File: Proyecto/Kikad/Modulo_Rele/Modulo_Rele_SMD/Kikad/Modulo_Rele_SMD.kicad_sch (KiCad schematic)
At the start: 8 parts, among them J1 TB_1X3, J2 TB_1X3, K1 RELAY_C, Q1 BC337, U3 PC817

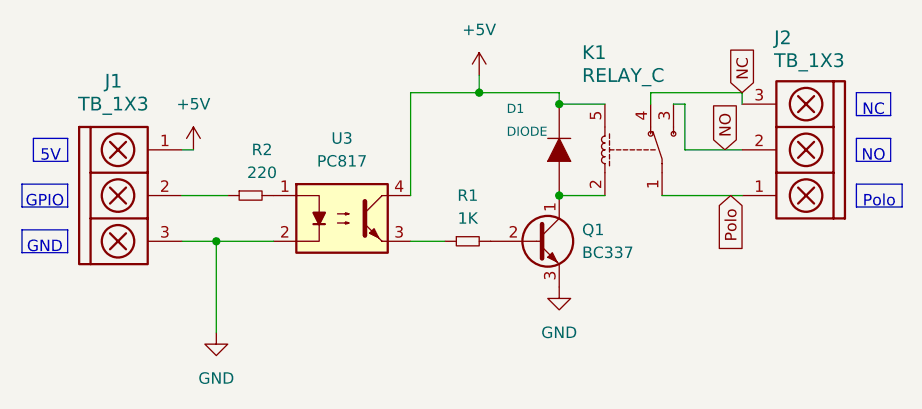
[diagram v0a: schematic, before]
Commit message: Hice el Modulo_Rele con SMD y adjunte las imagenes del mismo
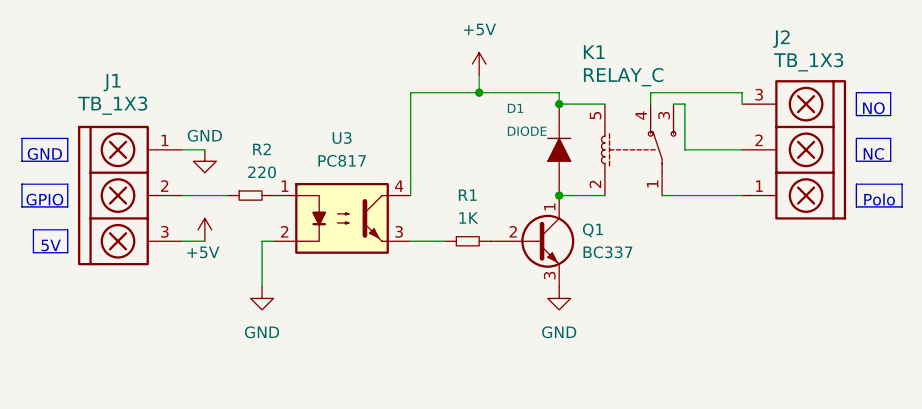
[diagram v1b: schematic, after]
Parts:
- D1: footprint Diode_THT:D_5W_P12.70mm_Horizontal -> Diode_SMD:D_SMA
- J1, J2: footprint Connector_PinHeader_2.54mm:PinHeader_1x03_P2.54mm_Vertical -> Connector_Molex:Molex_KK-254_AE-6410-03A_1x03_P2.54mm_Vertical
- Q1: footprint Package_TO_SOT_THT:TO-92_Inline -> Package_TO_SOT_SMD:SOT-23
- R1, R2: footprint Resistor_THT:R_Axial_DIN0207_L6.3mm_D2.5mm_P10.16mm_Horizontal -> Diode_SMD:D_0805_2012Metric
- U3: footprint Package_DIP:DIP-4_W7.62mm -> Package_SO:SSO-4_6.7x5.1mm_P2.54mm_Clearance8mm
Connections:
- net +5V: now also J1.3; no longer J1.1
- net GND: now also J1.1; no longer J1.3
- net NC: no longer names the net of J2.3, K1.4
- net NO: no longer names the net of J2.2, K1.3
- net Polo: no longer names the net of J2.1, K1.1

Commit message: hice el Rele Mixto y adjunte sus imagenes. ademas agregue la resistencia de 10K
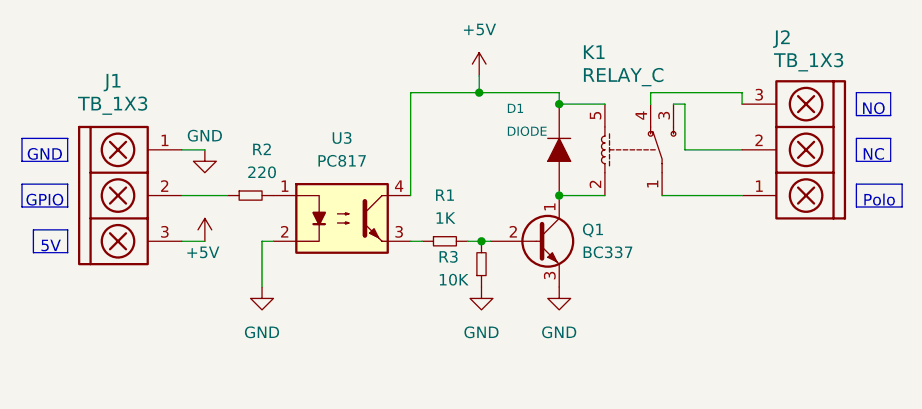
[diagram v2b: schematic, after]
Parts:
- added R3: 10K, EESTN5:R_0805, symbol EESTN5:R
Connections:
- net GND: now also R3.1
- net at Q1.2 (B), R1.2: now also R3.2
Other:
- moved on the sheet: R1
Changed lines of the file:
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@@
+	)
+	(junction
+		(at 139.954 78.74)
+		(diameter 0)
+		(color 0 0 0 0)
 	)
 	(junction
@@
 	(wire
 		(pts
+			(xy 139.954 78.74) (xy 140.97 78.74)
+		)
+		(stroke
+			(width 0)
+			(type default)
+		)
+	)
+	(wire
+		(pts
 			(xy 161.29 63.5) (xy 162.56 63.5)
 		)
@@
 	(wire
 		(pts
+			(xy 138.43 78.74) (xy 139.954 78.74)
+		)
+		(stroke
+			(width 0)
+			(type default)
+		)
+	)
+	(wire
+		(pts
 			(xy 132.08 73.66) (xy 132.08 62.23)
 		)
@@
 	(wire
 		(pts
-			(xy 132.08 78.74) (xy 135.89 78.74)
+			(xy 132.08 78.74) (xy 133.35 78.74)
 		)
 		(stroke
@@
 		)
 		(instances
-			(project "Modulo_Rele"
+			(project "Modulo_Rele_SMD"
 				(path "/ea0a02fe-b616-46a0-b0cf-00b16e0dffe3"
 					(reference "U3")
+					(unit 1)
+				)
+			)
+		)
+	)
+	(symbol
+		(lib_id "EESTN5:R")
+		(at 139.954 81.28 180)
+		(unit 1)
+		(exclude_from_sim no)
+		(in_bom yes)
+		(on_board yes)
+		(dnp no)
+		(property "Reference" "R3"
+			(at 135.128 80.518 0)
+			(effects
+				(font
+					(size 1.27 1.27)
+				)
+				(justify right)
+			)
+		)
+		(property "Value" "10K"
+			(at 135.128 83.058 0)
+			(effects
+				(font
+					(size 1.27 1.27)
+				)
+				(justify right)
+			)
+		)
+		(property "Footprint" "EESTN5:R_0805"
+			(at 139.954 81.28 0)
+			(effects
+				(font
+					(size 1.524 1.524)
+				)
+				(hide yes)
+			)
+		)
+		(property "Datasheet" ""
+			(at 139.954 81.28 0)
+			(effects
+				(font
+					(size 1.524 1.524)
+				)
+			)
+		)
+		(property "Description" "Resistor"
+			(at 139.954 81.28 0)
+			(effects
+				(font
+					(size 1.27 1.27)
+				)
+				(hide yes)
+			)
+		)
+		(pin "1"
+		)
+		(pin "2"
+		)
+		(instances
+			(project "Modulo_Rele_SMD"
+				(path "/ea0a02fe-b616-46a0-b0cf-00b16e0dffe3"
+					(reference "R3")
 					(unit 1)
 				)
@@
 		)
 		(instances
-			(project "Modulo_Rele"
+			(project "Modulo_Rele_SMD"
 				(path "/ea0a02fe-b616-46a0-b0cf-00b16e0dffe3"
 					(reference "J1")
@@
 	(symbol
 		(lib_id "EESTN5:R")
-		(at 138.43 78.74 90)
+		(at 135.89 78.74 90)
 		(unit 1)
 		(exclude_from_sim no)
@@
 		(fields_autoplaced yes)
 		(property "Reference" "R1"
-			(at 138.43 73.66 90)
+			(at 135.89 73.66 90)
 			(effects
 				(font
@@
 		)
 		(property "Value" "1K"
-			(at 138.43 76.2 90)
+			(at 135.89 76.2 90)
 			(effects
 				(font
@@
 		)
 		(property "Footprint" "Diode_SMD:D_0805_2012Metric"
-			(at 138.43 78.74 0)
+			(at 135.89 78.74 0)
 			(effects
 				(font
@@
 		)
 		(property "Datasheet" ""
-			(at 138.43 78.74 0)
+			(at 135.89 78.74 0)
 			(effects
 				(font
@@
 		)
 		(property "Description" "Resistor"
-			(at 138.43 78.74 0)
+			(at 135.89 78.74 0)
 			(effects
 				(font
@@
 		)
 		(instances
-			(project "Modulo_Rele"
+			(project "Modulo_Rele_SMD"
 				(path "/ea0a02fe-b616-46a0-b0cf-00b16e0dffe3"
 					(reference "R1")
@@
 		)
 		(instances
-			(project "Modulo_Rele"
+			(project "Modulo_Rele_SMD"
 				(path "/ea0a02fe-b616-46a0-b0cf-00b16e0dffe3"
 					(reference "#PWR05")
@@
 		)
 		(instances
-			(project "Modulo_Rele"
+			(project "Modulo_Rele_SMD"
 				(path "/ea0a02fe-b616-46a0-b0cf-00b16e0dffe3"
 					(reference "#PWR02")
@@
 		)
 		(instances
-			(project "Modulo_Rele"
+			(project "Modulo_Rele_SMD"
 				(path "/ea0a02fe-b616-46a0-b0cf-00b16e0dffe3"
 					(reference "J2")
@@
 		)
 		(instances
-			(project "Modulo_Rele"
+			(project "Modulo_Rele_SMD"
 				(path "/ea0a02fe-b616-46a0-b0cf-00b16e0dffe3"
 					(reference "#PWR03")
@@
 		)
 		(instances
-			(project "Modulo_Rele"
+			(project "Modulo_Rele_SMD"
 				(path "/ea0a02fe-b616-46a0-b0cf-00b16e0dffe3"
 					(reference "R2")
@@
 		)
 		(instances
-			(project "Modulo_Rele"
+			(project "Modulo_Rele_SMD"
 				(path "/ea0a02fe-b616-46a0-b0cf-00b16e0dffe3"
 					(reference "#PWR04")
@@
 		)
 		(instances
-			(project "Modulo_Rele"
+			(project "Modulo_Rele_SMD"
 				(path "/ea0a02fe-b616-46a0-b0cf-00b16e0dffe3"
 					(reference "#PWR01")
@@
 		)
 		(instances
-			(project "Modulo_Rele"
+			(project "Modulo_Rele_SMD"
 				(path "/ea0a02fe-b616-46a0-b0cf-00b16e0dffe3"
 					(reference "Q1")
@@
 		)
 		(instances
-			(project "Modulo_Rele"
+			(project "Modulo_Rele_SMD"
 				(path "/ea0a02fe-b616-46a0-b0cf-00b16e0dffe3"
 					(reference "D1")
+					(unit 1)
+				)
+			)
+		)
+	)
+	(symbol
+		(lib_id "power:GND")
+		(at 139.954 83.82 0)
+		(unit 1)
+		(exclude_from_sim no)
+		(in_bom yes)
+		(on_board yes)
+		(dnp no)
+		(fields_autoplaced yes)
+		(property "Reference" "#PWR06"
+			(at 139.954 90.17 0)
+			(effects
+				(font
+					(size 1.27 1.27)
+				)
+				(hide yes)
+			)
+		)
+		(property "Value" "GND"
+			(at 139.954 88.9 0)
+			(effects
+				(font
+					(size 1.27 1.27)
+				)
+			)
+		)
+		(property "Footprint" ""
+			(at 139.954 83.82 0)
+			(effects
+				(font
+					(size 1.27 1.27)
+				)
+				(hide yes)
+			)
+		)
+		(property "Datasheet" ""
+			(at 139.954 83.82 0)
+			(effects
+				(font
+					(size 1.27 1.27)
+				)
+				(hide yes)
+			)
+		)
+		(property "Description" "Power symbol creates a global label with name \"GND\" , ground"
+			(at 139.954 83.82 0)
+			(effects
+				(font
+					(size 1.27 1.27)
+				)
+				(hide yes)
+			)
+		)
+		(pin "1"
+		)
+		(instances
+			(project "Modulo_Rele_SMD"
+				(path "/ea0a02fe-b616-46a0-b0cf-00b16e0dffe3"
+					(reference "#PWR06")
 					(unit 1)
 				)
@@
 		)
 		(instances
-			(project "Modulo_Rele"
+			(project "Modulo_Rele_SMD"
 				(path "/ea0a02fe-b616-46a0-b0cf-00b16e0dffe3"
 					(reference "K1")

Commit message: Agregue la carpeta Placa_Principal e hice unas correcciones en el Modulo_Rele
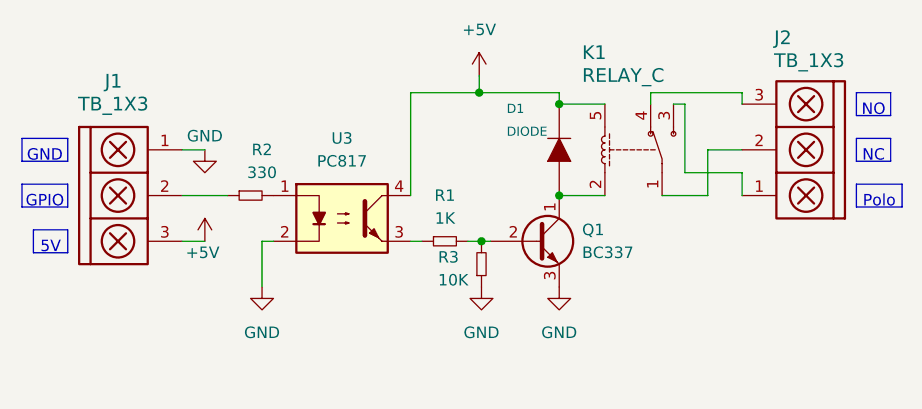
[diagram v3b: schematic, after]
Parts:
- J2: footprint Connector_Molex:Molex_KK-254_AE-6410-03A_1x03_P2.54mm_Vertical -> TerminalBlock:TerminalBlock_bornier-3_P5.08mm
- R2: value 220 -> 330
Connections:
- net at J2.1: now also K1.3; no longer K1.1
- net at J2.2: now also K1.1; no longer K1.3
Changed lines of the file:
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@@
-	(wire
-		(pts
-			(xy 160.02 73.66) (xy 168.91 73.66)
-		)
-		(stroke
-			(width 0)
-			(type default)
-		)
-	)
 	(wire
 		(pts
@@
 	(wire
 		(pts
+			(xy 168.91 68.58) (xy 165.1 68.58)
+		)
+		(stroke
+			(width 0)
+			(type default)
+		)
+	)
+	(wire
+		(pts
 			(xy 161.29 63.5) (xy 162.56 63.5)
 		)
@@
 	(wire
 		(pts
+			(xy 168.91 71.12) (xy 162.56 71.12)
+		)
+		(stroke
+			(width 0)
+			(type default)
+		)
+	)
+	(wire
+		(pts
 			(xy 132.08 73.66) (xy 132.08 62.23)
 		)
@@
 	(wire
 		(pts
-			(xy 162.56 63.5) (xy 162.56 68.58)
-		)
-		(stroke
-			(width 0)
-			(type default)
-		)
-	)
-	(wire
-		(pts
-			(xy 162.56 68.58) (xy 168.91 68.58)
+			(xy 162.56 63.5) (xy 162.56 71.12)
+		)
+		(stroke
+			(width 0)
+			(type default)
+		)
+	)
+	(wire
+		(pts
+			(xy 168.91 73.66) (xy 168.91 71.12)
 		)
 		(stroke
@@
 	(wire
 		(pts
+			(xy 165.1 68.58) (xy 165.1 73.66)
+		)
+		(stroke
+			(width 0)
+			(type default)
+		)
+	)
+	(wire
+		(pts
 			(xy 115.57 78.74) (xy 116.84 78.74)
+		)
+		(stroke
+			(width 0)
+			(type default)
+		)
+	)
+	(wire
+		(pts
+			(xy 160.02 73.66) (xy 165.1 73.66)
 		)
 		(stroke
@@
 			)
 		)
-		(property "Footprint" "Connector_Molex:Molex_KK-254_AE-6410-03A_1x03_P2.54mm_Vertical"
+		(property "Footprint" "TerminalBlock:TerminalBlock_bornier-3_P5.08mm"
 			(at 185.42 54.102 0)
 			(effects
@@
 			)
 		)
-		(property "Value" "220"
+		(property "Value" "330"
 			(at 115.57 71.12 90)
 			(effects
